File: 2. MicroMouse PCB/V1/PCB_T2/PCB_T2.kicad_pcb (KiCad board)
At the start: 2 copper layers, 70 x 70 mm, 18 parts, among them U1 STM32F407VGTx, Y1 48MHz

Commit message: update PCB 12/08/2024
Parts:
- removed L1: 10uH, Capacitor_SMD:C_0805_2012Metric_Pad1.18x1.45mm_HandSolder
- added C12: 15pF, Capacitor_SMD:C_0402_1005Metric, B.Cu at (152.7, 108.9)
- added C13: 15pF, Capacitor_SMD:C_0402_1005Metric, B.Cu at (152.8, 101.8)
- added C14: 100nF, Capacitor_SMD:C_0402_1005Metric, B.Cu at (166.6, 106.4)
- added C15: 100nF, Capacitor_SMD:C_0402_1005Metric, B.Cu at (109.2, 103.9)
- added C16: 100nF, Capacitor_SMD:C_0402_1005Metric, B.Cu at (109.3, 105.8)
- added D0: 3VL, LED_SMD:LED_0603_1608Metric, F.Cu at (129.2, 117.8)
- added D1: 3VL, LED_SMD:LED_0603_1608Metric, F.Cu at (136.0, 117.8)
- added D2: 3VL, LED_SMD:LED_0603_1608Metric, F.Cu at (142.6, 117.8)
- added D3: 3VL, LED_SMD:LED_0603_1608Metric, F.Cu at (149.3, 117.8)
- added J1: MPU, Connector_PinHeader_2.54mm:PinHeader_1x04_P2.54mm_Vertical, F.Cu at (133.3, 83.9)
- added J10: Conn_01x26_Socket, Connector_FFC-FPC:Hirose_FH12-26S-0.5SH_1x26-1MP_P0.50mm_Horizontal, F.Cu at (141.3, 77.0)
- added J2: MPU, Connector_JST:JST_SH_BM04B-SRSS-TB_1x04-1MP_P1.00mm_Vertical, F.Cu at (161.1, 101.7)
- added J3: MPU, Connector_JST:JST_SH_BM04B-SRSS-TB_1x04-1MP_P1.00mm_Vertical, F.Cu at (119.2, 101.2)
- added J4: MPU, Connector_JST:JST_SH_BM04B-SRSS-TB_1x04-1MP_P1.00mm_Vertical, F.Cu at (161.1, 108.4)
- added J6: Conn_01x03_Pin, Connector_JST:JST_SH_BM03B-SRSS-TB_1x03-1MP_P1.00mm_Vertical, F.Cu at (109.5, 101.5)
- added J7: Conn_01x03_Pin, Connector_JST:JST_SH_BM03B-SRSS-TB_1x03-1MP_P1.00mm_Vertical, F.Cu at (109.5, 107.8)
- added J8: Conn_01x03_Pin, Connector_JST:JST_SH_BM03B-SRSS-TB_1x03-1MP_P1.00mm_Vertical, F.Cu at (168.9, 108.4)
- added J9: Conn_01x03_Pin, Connector_JST:JST_SH_BM03B-SRSS-TB_1x03-1MP_P1.00mm_Vertical, F.Cu at (169.0, 101.7)
- added RN1: R_Pack04, Resistor_SMD:R_Array_Convex_4x0603, B.Cu at (139.1, 122.4)
- added STLINK1: STLINK, Connector_JST:JST_SH_SM04B-SRSS-TB_1x04-1MP_P1.00mm_Horizontal, F.Cu at (119.2, 107.8)
- added SW1: SW_Push, Button_Switch_SMD:SW_Tactile_SPST_NO_Straight_CK_PTS636Sx25SMTRLFS, B.Cu at (168.9, 109.0)
- added SW2: SW_Push, Button_Switch_SMD:SW_Tactile_SPST_NO_Straight_CK_PTS636Sx25SMTRLFS, B.Cu at (111.7, 101.1)
- added SW3: SW_Push, Button_Switch_SMD:SW_Tactile_SPST_NO_Straight_CK_PTS636Sx25SMTRLFS, B.Cu at (111.7, 108.6)
- added U2: Output 3.3V, Mini560:Mini560_5A, F.Cu at (139.0, 130.3)
- C1, C3: value 100nF -> 2.2uF; footprint Capacitor_SMD:C_0603_1608Metric -> Capacitor_Tantalum_SMD:CP_EIA-3216-10_Kemet-I; moved to B.Cu
- C10, C11: value 20pF -> 100nF; footprint Capacitor_SMD:C_0603_1608Metric -> Capacitor_SMD:C_0402_1005Metric; moved to B.Cu
- C2, C4, C5, C6, C7, C8: footprint Capacitor_SMD:C_0603_1608Metric -> Capacitor_SMD:C_0402_1005Metric; moved to B.Cu
- C9: value 100nF -> 4.7uF; footprint Capacitor_SMD:C_0603_1608Metric -> Capacitor_Tantalum_SMD:CP_EIA-3216-10_Kemet-I; moved to B.Cu
- R1, R2: value 4.7K -> 1K; footprint Resistor_SMD:R_0603_1608Metric -> Resistor_SMD:R_0402_1005Metric; moved to B.Cu
- R3, R4: footprint Resistor_SMD:R_0603_1608Metric -> Resistor_SMD:R_0402_1005Metric; moved to B.Cu
- U1: value STM32F407VGTx -> STM32H743VIT6
- Y1: moved to B.Cu
- moved R2 47.8 mm to (114.1, 105.8), turned to 180 degrees
- moved R3 44.8 mm to (120.1, 111.0)
- moved R4 42.0 mm to (118.7, 107.5), turned to 180 degrees
- moved R1 37.4 mm to (114.0, 103.9), turned to 180 degrees
- moved C2 34.5 mm to (128.6, 111.1), turned to -90 degrees
- moved Y1 31.7 mm to (154.4, 105.3), turned to 90 degrees
- moved C3 31.5 mm to (126.8, 108.9)
- moved C4 27.3 mm to (147.4, 113.1), turned to 90 degrees
- moved C1 24.3 mm to (129.4, 97.0)
- moved C7 24.0 mm to (150.8, 102.2), turned to 90 degrees
- moved C10 23.7 mm to (129.3, 98.8)
- moved C11 23.3 mm to (129.3, 100.5), turned to 180 degrees
- moved C5 21.2 mm to (150.5, 108.9)
- moved C8 19.6 mm to (150.8, 100.3), turned to -90 degrees
- moved C6 17.5 mm to (150.5, 107.5)
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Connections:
- C10 pad 2: /PH0 -> +3.3V
- C11 pad 1: GND -> +3.3V
- C11 pad 2: /PH1 -> GND
- C2 pad 1: +3.3V -> GND
- C2 pad 2: Net-(C2-Pad2) -> +3.3V
- C6 pad 1: GND -> +3.3V
- C6 pad 2: Net-(U1-VBAT) -> GND
- R1 pad 1: /SCL -> /BUTTON_1
- R2 pad 1: /SDA -> /BUTTON_2
- R3 pad 2: VCC -> +3.3V
- R4 pad 1: /SWDIO -> GND
- R4 pad 2: GND -> /SWDIO
- U1 pad 15: unconnected-(U1-PC0-Pad15) -> /N_TOF
- U1 pad 16: unconnected-(U1-PC1-Pad16) -> /W_TOF
- U1 pad 17: unconnected-(U1-PC2-Pad17) -> /S_TOF
- U1 pad 18: unconnected-(U1-PC3-Pad18) -> /E_TOF
- U1 pad 21: Net-(U1-VREF+) -> +3.3V
- U1 pad 23: unconnected-(U1-PA0-Pad23) -> /NE_ENC_A
- U1 pad 24: unconnected-(U1-PA1-Pad24) -> /NE_ENC_B
- U1 pad 25: unconnected-(U1-PA2-Pad25) -> /USART2_TX
- U1 pad 26: unconnected-(U1-PA3-Pad26) -> /USART2_RX
- U1 pad 30: unconnected-(U1-PA5-Pad30) -> /NW_ENC_A
- U1 pad 31: unconnected-(U1-PA6-Pad31) -> /SW_ENC_A
- U1 pad 32: unconnected-(U1-PA7-Pad32) -> /SW_ENC_B
- U1 pad 35: unconnected-(U1-PB0-Pad35) -> /NW_IN1
- U1 pad 36: unconnected-(U1-PB1-Pad36) -> /NW_IN2
- U1 pad 37: unconnected-(U1-PB2-Pad37) -> /SW_IN1
- U1 pad 38: unconnected-(U1-PE7-Pad38) -> /SW_IN2
- U1 pad 39: unconnected-(U1-PE8-Pad39) -> /SE_IN1
- U1 pad 40: unconnected-(U1-PE9-Pad40) -> /NW_PWM
- U1 pad 41: unconnected-(U1-PE10-Pad41) -> /SE_IN2
- U1 pad 42: unconnected-(U1-PE11-Pad42) -> /SW_PWM
- U1 pad 43: unconnected-(U1-PE12-Pad43) -> /NE_IN1
- U1 pad 44: unconnected-(U1-PE13-Pad44) -> /SE_PWM
- U1 pad 45: unconnected-(U1-PE14-Pad45) -> /NE_PWM
- U1 pad 46: unconnected-(U1-PE15-Pad46) -> /NE_IN2
- U1 pad 53: unconnected-(U1-PB14-Pad53) -> /USART1_TX
- U1 pad 54: unconnected-(U1-PB15-Pad54) -> /USART1_RX
- U1 pad 55: unconnected-(U1-PD8-Pad55) -> /USART3_TX
- U1 pad 56: unconnected-(U1-PD9-Pad56) -> /USART3_RX
- U1 pad 59: unconnected-(U1-PD12-Pad59) -> /SE_ENC_A
- U1 pad 6: Net-(U1-VBAT) -> +3.3V
- U1 pad 60: unconnected-(U1-PD13-Pad60) -> /SE_ENC_B
- U1 pad 63: unconnected-(U1-PC6-Pad63) -> /NW_SERVO
- U1 pad 64: unconnected-(U1-PC7-Pad64) -> /SW_SERVO
- U1 pad 65: unconnected-(U1-PC8-Pad65) -> /SE_SERVO
- U1 pad 66: unconnected-(U1-PC9-Pad66) -> /NE_SERVO
- U1 pad 81: unconnected-(U1-PD0-Pad81) -> /BUTTON_0
- U1 pad 82: unconnected-(U1-PD1-Pad82) -> /BUTTON_1
- U1 pad 83: unconnected-(U1-PD2-Pad83) -> /LED_0
- U1 pad 84: unconnected-(U1-PD3-Pad84) -> /LED_1
- U1 pad 85: unconnected-(U1-PD4-Pad85) -> /LED_2
- U1 pad 86: unconnected-(U1-PD5-Pad86) -> /LED_3
- U1 pad 89: unconnected-(U1-PB3-Pad89) -> /NW_ENC_B
- U1 pad 92: /SCL -> /I2C1_SCL
- U1 pad 93: unconnected-(U1-PB7-Pad93) -> /I2C1_SDA
- U1 pad 95: unconnected-(U1-PB8-Pad95) -> /I2C4_SCL
- U1 pad 96: /SDA -> /I2C4_SDA
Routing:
- net +3.3V: track 0.00 -> 97.5 mm, vias 0 -> 5
- net /NE_SERVO: track 0.00 -> 45.6 mm, vias 0 -> 2
- net /SE_SERVO: track 0.00 -> 43.0 mm
- net /NW_ENC_B: track 0.00 -> 36.0 mm, vias 0 -> 2
- net /BUTTON_1: track 0.00 -> 31.6 mm, vias 0 -> 1
- net /I2C1_SCL: track 0.00 -> 30.0 mm
- net /SE_ENC_B: track 0.00 -> 29.1 mm, vias 0 -> 2
- net /N_TOF: track 0.00 -> 28.7 mm
- net /SE_ENC_A: track 0.00 -> 28.1 mm
- net /W_TOF: track 0.00 -> 27.8 mm
- net /S_TOF: track 0.00 -> 27.0 mm
- net /NE_ENC_A: track 0.00 -> 26.5 mm, vias 0 -> 2
- net /NE_ENC_B: track 0.00 -> 26.1 mm, vias 0 -> 2
- net /E_TOF: track 0.00 -> 26.1 mm
- net /SW_SERVO: track 0.00 -> 25.0 mm
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
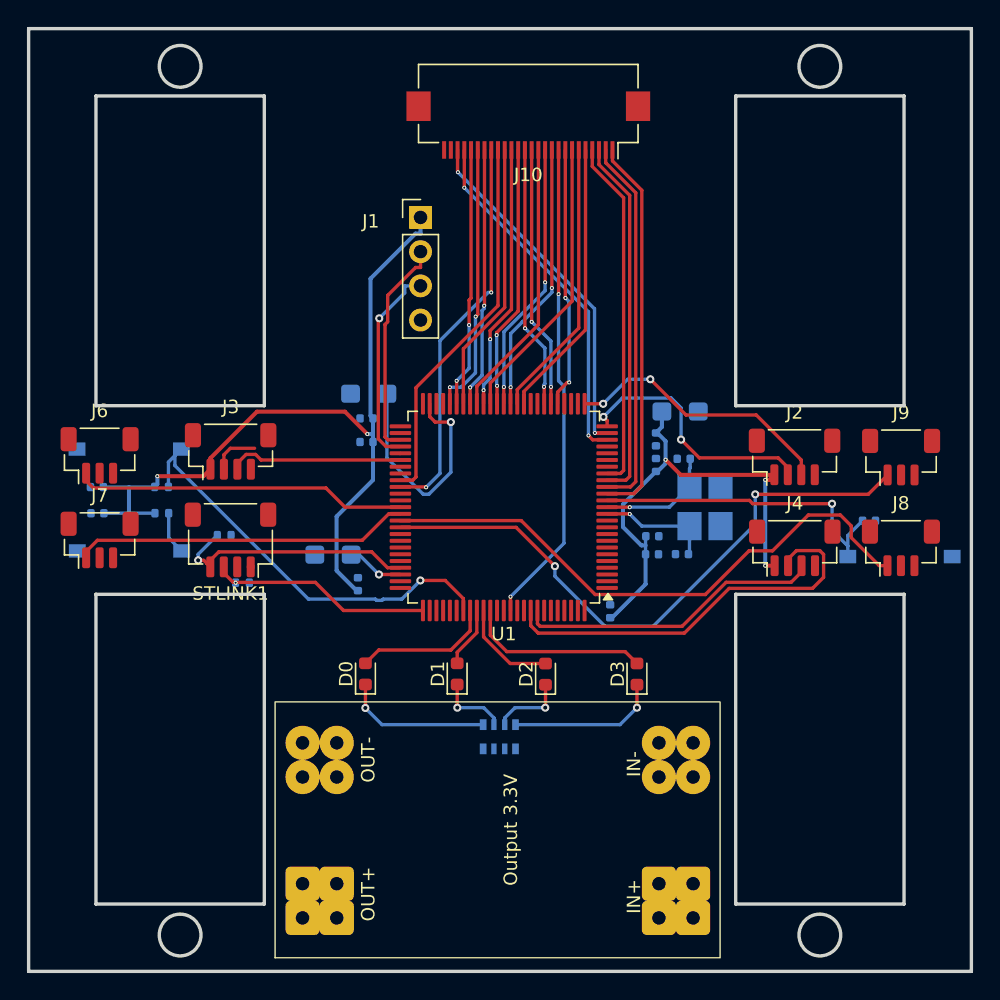
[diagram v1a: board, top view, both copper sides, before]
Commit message: update route tracks before change
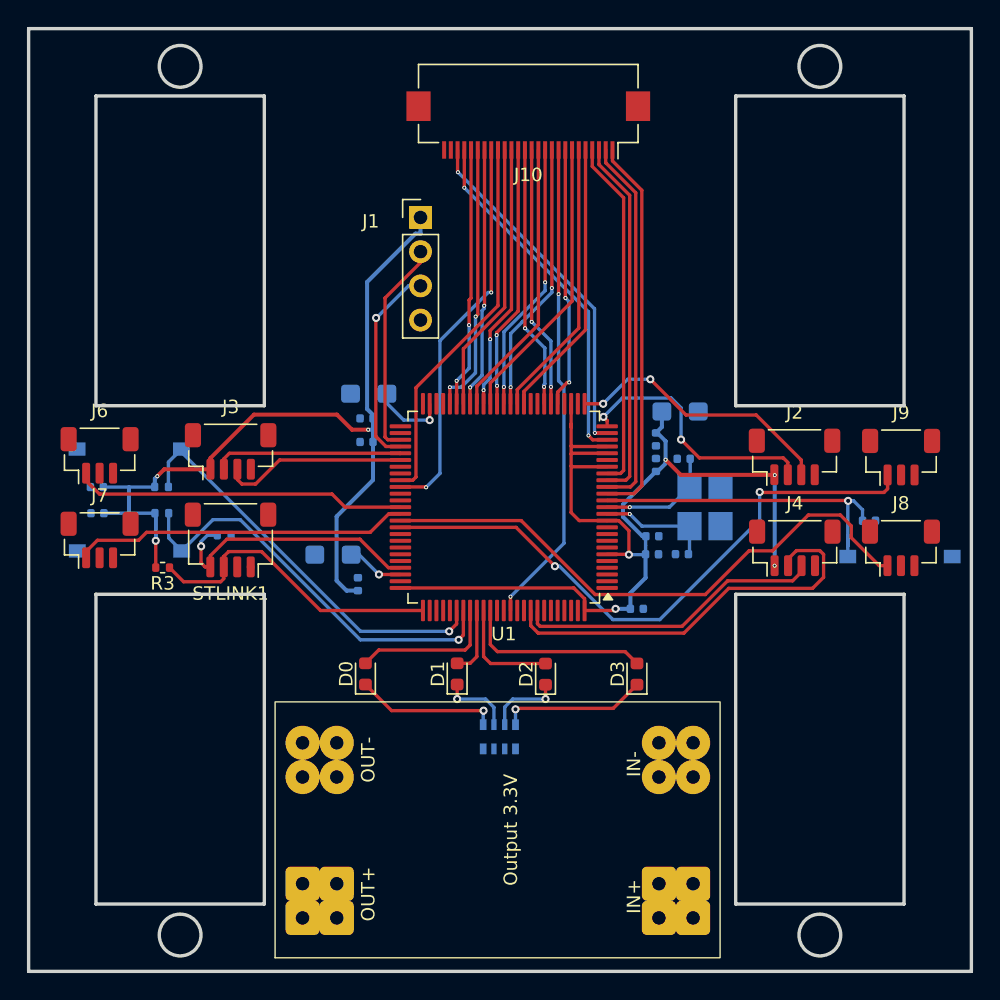
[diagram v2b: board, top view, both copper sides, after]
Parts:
- R3: moved to F.Cu
- moved R3 6.03 mm to (114.1, 109.9), turned to 180 degrees
- moved C4 1.99 mm to (149.3, 112.9), turned to 0 degrees
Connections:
- R1 pad 1: /BUTTON_1 -> /BUTTON_0
- R2 pad 1: /BUTTON_2 -> /BUTTON_1
- SW2 pad 2: /BUTTON_1 -> /BUTTON_0
- SW3 pad 2: /BUTTON_2 -> /BUTTON_1
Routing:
- net +3.3V: track 97.5 -> 145.0 mm, vias 5 -> 8
- net /BUTTON_0: track 0.00 -> 30.6 mm, vias 0 -> 1
- net Net-(U1-VCAP_1): track 17.7 -> 5.62 mm
- net /USART3_TX: track 3.59 -> 14.1 mm
- net /SWCLK: track 16.4 -> 23.0 mm, vias 1 -> 0
- net /BUTTON_2: track 3.20 -> 0.00 mm
- net /NRST: track 23.5 -> 25.0 mm
- net /SWDIO: track 18.8 -> 20.1 mm
- net /USART3_RX: track 13.0 -> 14.2 mm
- net /LED_2: track 7.38 -> 8.23 mm
- net /BUTTON_1: track 31.6 -> 30.7 mm
- net /LED_0: track 10.3 -> 10.9 mm
- net /LED_1: track 4.52 -> 5.09 mm

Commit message: completed schematic of all in one PCB
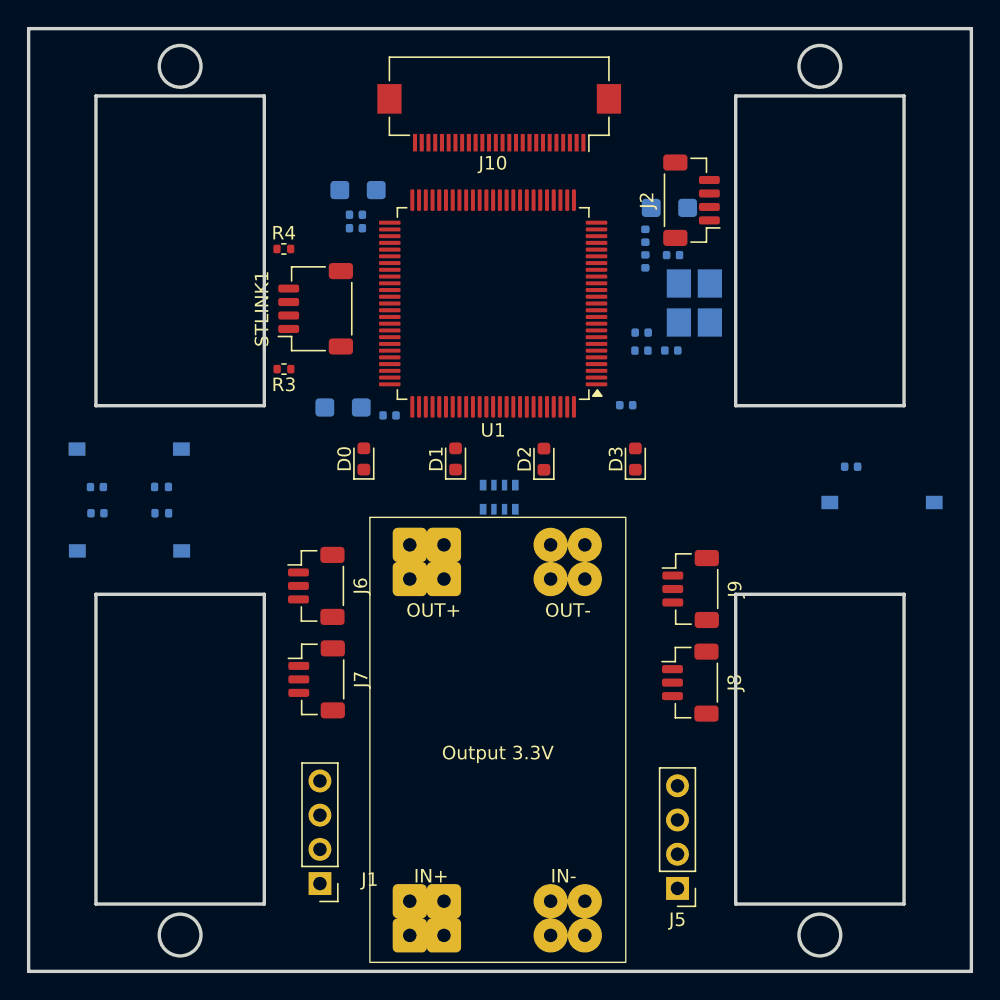
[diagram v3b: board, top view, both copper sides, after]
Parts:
- removed J3, J4: MPU, Connector_JST:JST_SH_BM04B-SRSS-TB_1x04-1MP_P1.00mm_Vertical
- added J5: Conn_01x04_Pin, Connector_PinHeader_2.54mm:PinHeader_1x04_P2.54mm_Vertical, F.Cu at (152.4, 133.7)
- R4: moved to F.Cu
- moved J1 50.0 mm to (125.8, 133.3), turned to 180 degrees
- moved R4 21.7 mm to (123.1, 86.2), turned to 0 degrees
- moved J2 20.5 mm to (153.4, 82.6), turned to 90 degrees
- moved J7 19.2 mm to (125.6, 118.2), turned to -90 degrees
- moved J6 18.8 mm to (125.5, 111.2), turned to -90 degrees
- moved J8 18.6 mm to (153.3, 118.4), turned to -90 degrees
- moved J9 18.4 mm to (153.3, 111.5), turned to -90 degrees
- moved STLINK1 18.3 mm to (125.5, 90.7), turned to 90 degrees
- moved RN1 17.8 mm to (139.1, 104.6)
- moved R3 17.3 mm to (123.1, 95.1)
- moved D0 16.0 mm to (129.1, 101.8)
- moved D1 16.0 mm to (135.9, 101.8)
- moved D2 16.0 mm to (142.4, 101.8)
- moved D3 16.0 mm to (149.2, 101.8)
- moved C11 15.9 mm to (128.5, 84.7)
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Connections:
- STLINK1 pad 1: +5V -> +3.3V
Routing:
- net +3.3V: track 145.0 -> 0.00 mm, vias 8 -> 0
- net /NE_SERVO: track 45.3 -> 0.00 mm, vias 2 -> 0
- net /SE_SERVO: track 43.0 -> 0.00 mm
- net /NW_ENC_B: track 36.0 -> 0.00 mm, vias 2 -> 0
- net /BUTTON_1: track 30.7 -> 0.00 mm, vias 1 -> 0
- net /BUTTON_0: track 30.6 -> 0.00 mm, vias 1 -> 0
- net /I2C1_SCL: track 30.0 -> 0.00 mm
- net /SE_ENC_B: track 29.1 -> 0.00 mm, vias 2 -> 0
- net /N_TOF: track 28.7 -> 0.00 mm
- net /SE_ENC_A: track 28.1 -> 0.00 mm
- net /W_TOF: track 27.8 -> 0.00 mm
- net /S_TOF: track 27.0 -> 0.00 mm
- net /NE_ENC_A: track 26.5 -> 0.00 mm, vias 2 -> 0
- net /NE_ENC_B: track 26.1 -> 0.00 mm, vias 2 -> 0
- net /E_TOF: track 26.1 -> 0.00 mm
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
